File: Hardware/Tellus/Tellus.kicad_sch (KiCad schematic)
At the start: 37 parts, among them J1 Conn_01x10_Female, J2 Conn_01x06_Female, J3 Conn_01x04_Female, J4 Conn_01x02_Female, M1 Motor_DC, M2 Motor_DC, M3 Motor_DC, M4 Motor_DC, M5 Motor_DC, M6 Motor_DC, U1 AMS1117-3.3, U2 ICM-42670-P, U3 MAX8815A, U4 MC6470, U5 LM7805_TO220, U6 A3909, U7 A3909, U8 A3909, U9 DEV-16771

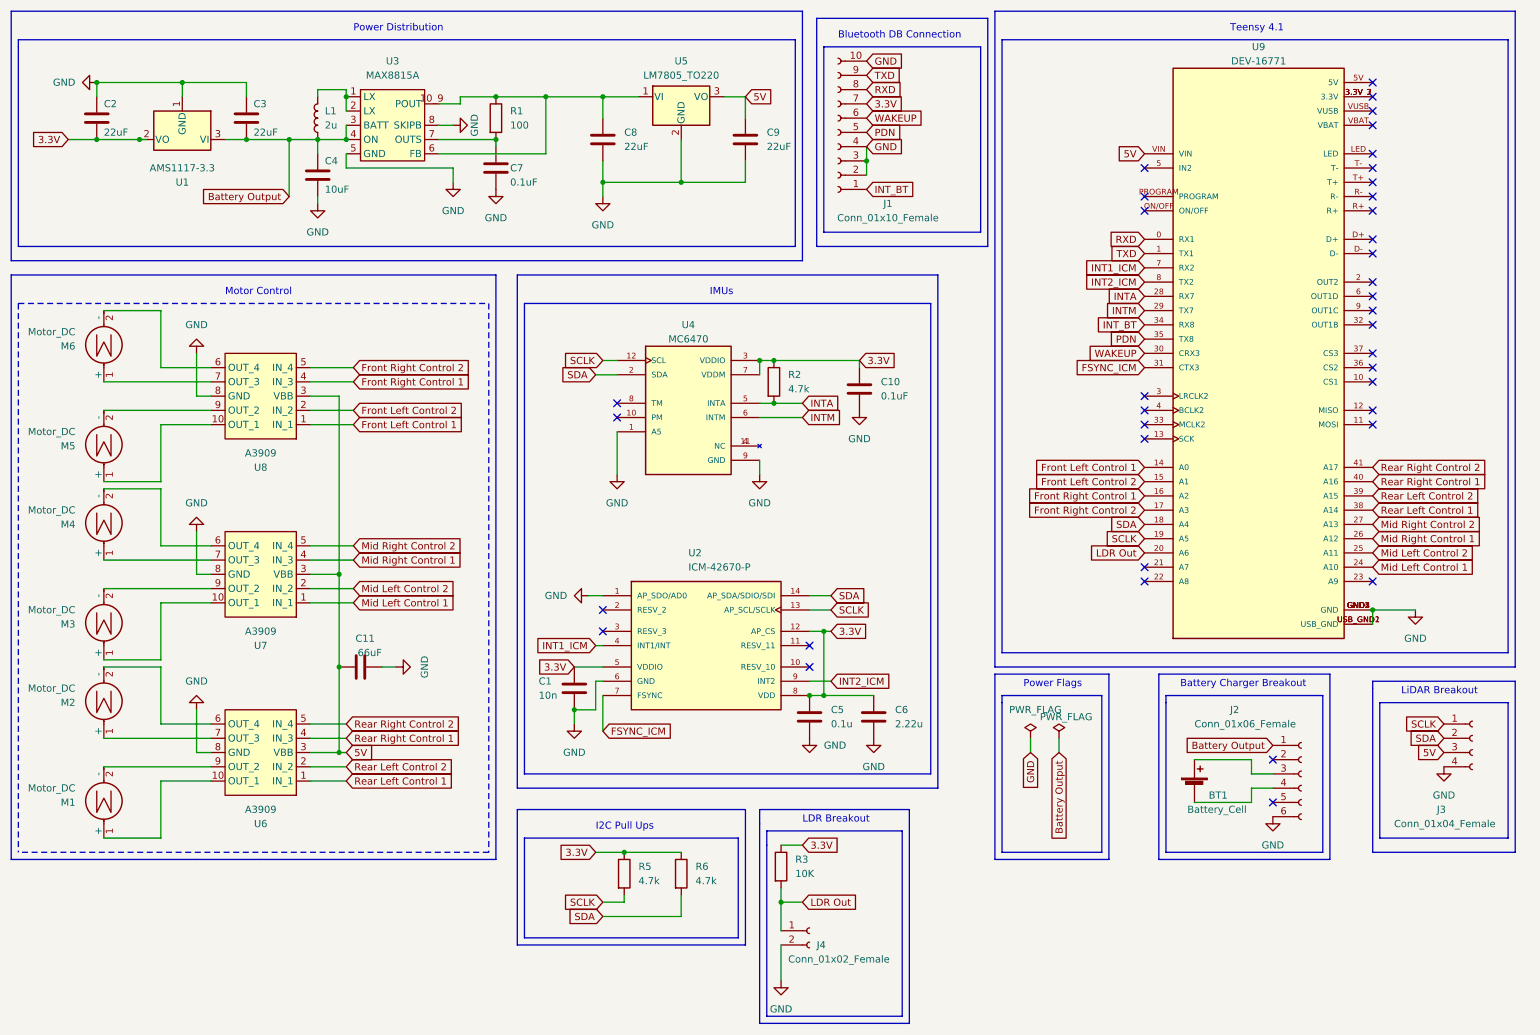
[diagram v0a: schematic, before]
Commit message: Merge robot config file additions from main to pathfinding_test (#30)
* Added Middle wheel control

* Add files via upload

* Add files via upload

* Add files via upload

* Add files via upload

* Add files via upload

* Update cooperative-scan.argos

* PCB Updates

Re-Layered PCB to match Signal, PWR, GND, Signal suggestion. Cleaned up power connections, Bluetooth saddle, and LiDAR mounts.

Fixed the following DRC Violations/Warnings:
No Footprint assigned for Mounting holes
- Fixed by adding them in the schematic.

Unconnected 3.3V Terminals on Teensy
- Fixed Symbol in schematic that had them on top of each other. The teensy spec does not recommend tying these together.

No net assigned for Motor Driver EP
-Modified Symbol in schematic to include the EP, and connected it to GND, as suggested in the data sheet.

* Added Logos

Added MSU Logo and Robotics Club Logo to the front and back silkscreen layers

* Cleanup

* Final Edits and Manufacturer File Generation

---------

Co-authored-by: Jacob Fifield <43118015+Fife@users.noreply.github.com>
Co-authored-by: Fife <jacob.m.fifield@gmail.com>
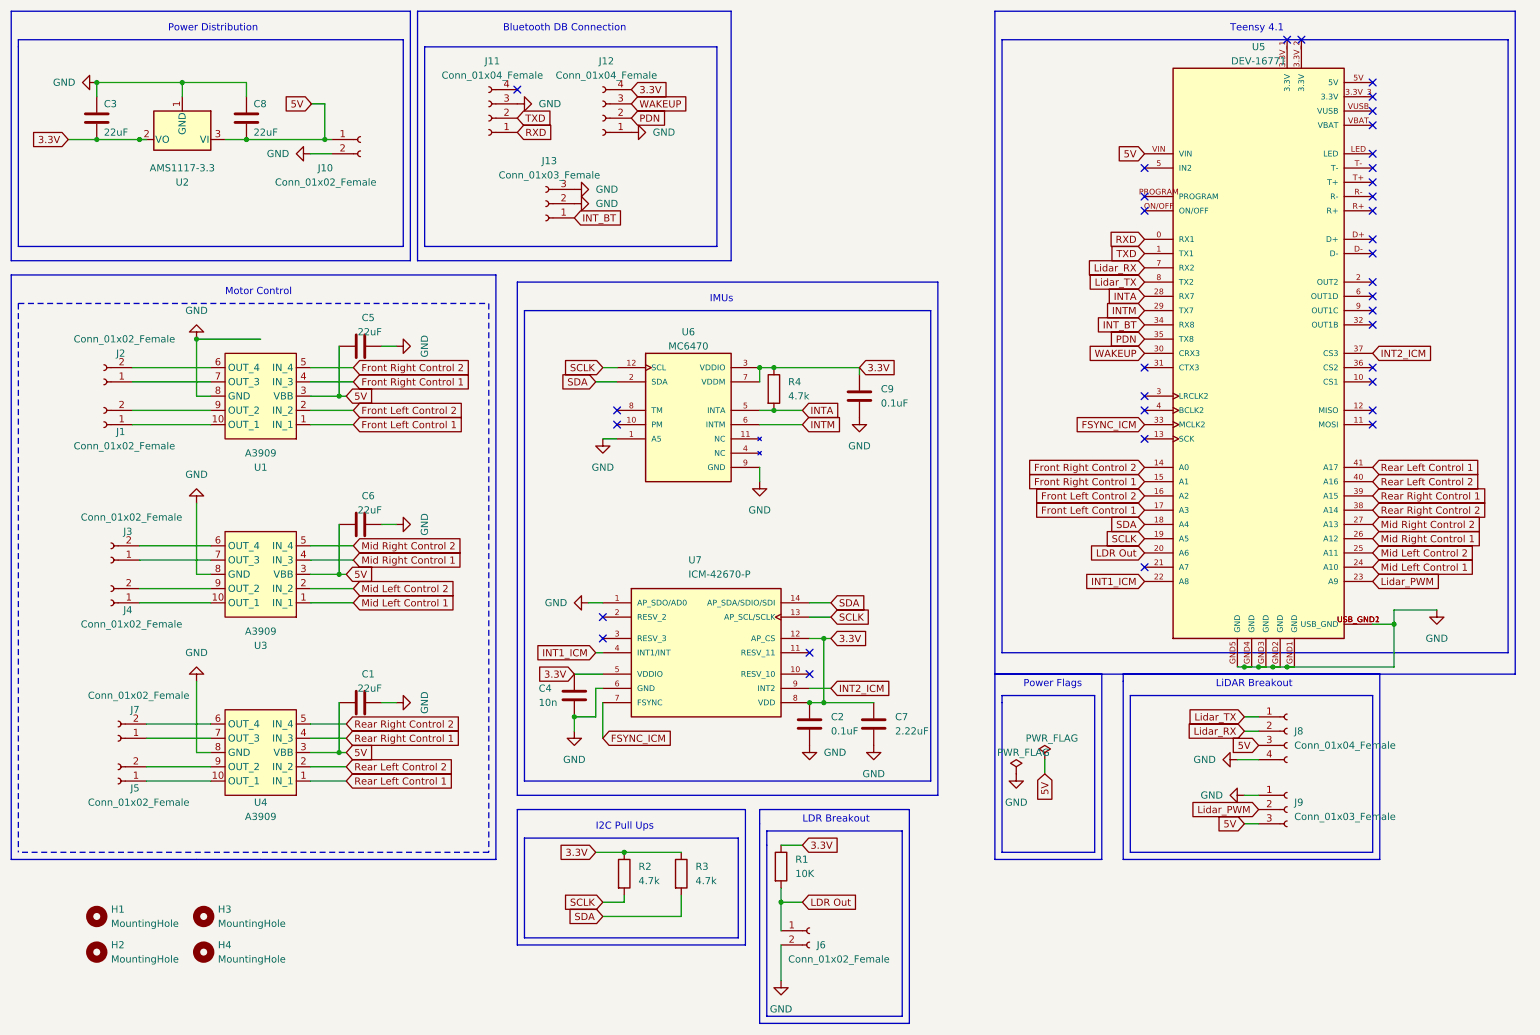
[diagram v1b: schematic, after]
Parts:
- removed BT1: Battery_Cell, symbol Device:Battery_Cell
- removed C4: 10uF, symbol Device:C
- removed C7: 0.1uF, symbol Device:C
- removed C8, C9: 22uF, symbol Device:C
- removed J1: Conn_01x10_Female, symbol Connector:Conn_01x10_Female
- removed J2: Conn_01x06_Female, symbol Connector:Conn_01x06_Female
- removed J3: Conn_01x04_Female, symbol Connector:Conn_01x04_Female
- removed L1: 2u, symbol Device:L
- removed M1, M2, M3, M4, M5, M6: Motor_DC, symbol Motor:Motor_DC
- removed R1: 100, symbol Device:R
- removed U3: MAX8815A, symbol BoostConverter:MAX8815A
- removed U5: LM7805_TO220, Package_TO_SOT_THT:TO-220-3_Vertical, symbol Regulator_Linear:LM7805_TO220
- added C5, C6: 22uF, Capacitor_SMD:C_1210_3225Metric_Pad1.33x2.70mm_HandSolder, symbol Device:C
- added H1, H2, H3, H4: MountingHole, symbol Mechanical:MountingHole
- added J1, J10, J2, J3, J4, J5, J7: Conn_01x02_Female, Connector_PinHeader_2.54mm:PinHeader_1x02_P2.54mm_Vertical, symbol Connector:Conn_01x02_Female
- added J11, J12: Conn_01x04_Female, Connector_PinHeader_2.00mm:PinHeader_1x04_P2.00mm_Vertical, symbol Connector:Conn_01x04_Female
- added J13: Conn_01x03_Female, Connector_PinHeader_2.00mm:PinHeader_1x03_P2.00mm_Vertical, symbol Connector:Conn_01x03_Female
- added J8: Conn_01x04_Female, Connector_PinHeader_2.54mm:PinHeader_1x04_P2.54mm_Vertical, symbol Connector:Conn_01x04_Female
- added J9: Conn_01x03_Female, Connector_PinHeader_2.54mm:PinHeader_1x03_P2.54mm_Vertical, symbol Connector:Conn_01x03_Female
- C1: renamed from C11; value 66uF -> 22uF; footprint (none) -> Capacitor_SMD:C_1210_3225Metric_Pad1.33x2.70mm_HandSolder
- C2: renamed from C5; value 0.1u -> 0.1uF; footprint (none) -> Capacitor_SMD:C_1210_3225Metric_Pad1.33x2.70mm_HandSolder
- C3: renamed from C2; footprint (none) -> Capacitor_SMD:C_1210_3225Metric_Pad1.33x2.70mm_HandSolder
- C4: renamed from C1; footprint (none) -> Capacitor_SMD:C_1210_3225Metric_Pad1.33x2.70mm_HandSolder
- C7: renamed from C6; value 2.22u -> 2.22uF; footprint (none) -> Capacitor_SMD:C_1210_3225Metric_Pad1.33x2.70mm_HandSolder
- C8: renamed from C3; footprint (none) -> Capacitor_SMD:C_1210_3225Metric_Pad1.33x2.70mm_HandSolder
- C9: renamed from C10; footprint (none) -> Capacitor_SMD:C_1210_3225Metric_Pad1.33x2.70mm_HandSolder
- J6: renamed from J4; footprint (none) -> Connector_PinHeader_2.54mm:PinHeader_1x02_P2.54mm_Vertical
- R1: renamed from R3; footprint (none) -> Resistor_SMD:R_1206_3216Metric
- R2: renamed from R5; footprint (none) -> Resistor_SMD:R_1206_3216Metric
- R3: renamed from R6; footprint (none) -> Resistor_SMD:R_1206_3216Metric
- R4: renamed from R2; footprint (none) -> Resistor_SMD:R_1206_3216Metric
- U1: renamed from U8; footprint (none) -> Package_SO:SSOP-10_3.9x4.9mm_P1.00mm
- U2: renamed from U1; footprint Package_TO_SOT_SMD:SOT-223-3_TabPin2 -> Package_TO_SOT_SMD:SOT-89-3
- U3: renamed from U7; footprint (none) -> Package_SO:SSOP-10_3.9x4.9mm_P1.00mm
- U4: renamed from U6; footprint (none) -> Package_SO:SSOP-10_3.9x4.9mm_P1.00mm
- U5: renamed from U9; footprint MODULE_DEV-16771 -> KicadLibs:MODULE_DEV-16771
- U6: renamed from U4; footprint PQFN50P200X200X100-12N -> KicadLibs:PQFN50P200X200X100-12N
- U7: renamed from U2; footprint IC_ICM-42670-P -> ICM42670P:IC_ICM-42670-P
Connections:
- net Battery Output is gone; now on net 5V: C8.2, U2.3 (VI)
- net 3.3V: now also J12.4 (Pin_4)
- net 5V: now also C5.1, C6.1, J10.1 (Pin_1), J8.3 (Pin_3), J9.3 (Pin_3)
- net FSYNC_ICM: now also U5.33 (MCLK2); no longer U5.31 (CTX3)
- net Front Left Control 1: now also U5.17 (A3); no longer U5.14 (A0)
- net Front Left Control 2: now also U5.16 (A2); no longer U5.15 (A1)
- net Front Right Control 1: now also U5.15 (A1); no longer U5.16 (A2)
- net Front Right Control 2: now also U5.14 (A0); no longer U5.17 (A3)
- net GND: now also C5.2, C6.2, J10.2 (Pin_2), J11.3 (Pin_3), J12.1 (Pin_1), J13.2 (Pin_2), J13.3 (Pin_3), J8.4 (Pin_4), J9.1 (Pin_1)
- net INT1_ICM: now also U5.22 (A8); no longer U5.7 (RX2)
- net INT2_ICM: now also U5.37 (CS3); no longer U5.8 (TX2)
- net INT_BT: now also J13.1 (Pin_1)
- net PDN: now also J12.2 (Pin_2)
- net RXD: now also J11.1 (Pin_1)
- net Rear Left Control 1: now also U5.41 (A17); no longer U5.38 (A14)
- net Rear Left Control 2: now also U5.40 (A16); no longer U5.39 (A15)
- net Rear Right Control 1: now also U5.39 (A15); no longer U5.40 (A16)
- net Rear Right Control 2: now also U5.38 (A14); no longer U5.41 (A17)
- net TXD: now also J11.2 (Pin_2)
- net WAKEUP: now also J12.3 (Pin_3)
- net at U1.10 (OUT_1): now also J1.1 (Pin_1)
- net at U1.6 (OUT_4): now also J2.2 (Pin_2)
- net at U1.7 (OUT_3): now also J2.1 (Pin_1)
- net at U1.9 (OUT_2): now also J1.2 (Pin_2)
- net at U3.10 (OUT_1): now also J4.1 (Pin_1)
- net at U3.9 (OUT_2): now also J4.2 (Pin_2)
- net at U6.11 (NC): no longer U6.4 (NC)
- net at U4.7 (OUT_3): now also J7.1 (Pin_1)
- net at U4.6 (OUT_4): now also J7.2 (Pin_2)
- net at U4.10 (OUT_1): now also J5.1 (Pin_1)
- net at U4.9 (OUT_2): now also J5.2 (Pin_2)
- net Lidar_PWM: now reaches U5.23 (A9)
- net Lidar_PWM: now also J9.2 (Pin_2)
- net at U3.6 (OUT_4): now also J3.2 (Pin_2)
- net at U3.7 (OUT_3): now also J3.1 (Pin_1)
- new net Lidar_RX: J8.2 (Pin_2), U5.7 (RX2)
- new net Lidar_TX: J8.1 (Pin_1), U5.8 (TX2)
- now unconnected: U5.3.3V_1 (3.3V), U5.3.3V_2 (3.3V), U5.3.3V_3 (3.3V)
- no-connect marks 38 -> 36
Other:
- note removed: "Battery Charger Breakout"
- moved on the sheet: C1, C2, C4, C7, C9, R4, U7
